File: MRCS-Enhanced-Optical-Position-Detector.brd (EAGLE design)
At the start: 45.6 x 30.3 mm, 17 parts, among them IC1 LM2903N, T1 PT19, T2 2N4401

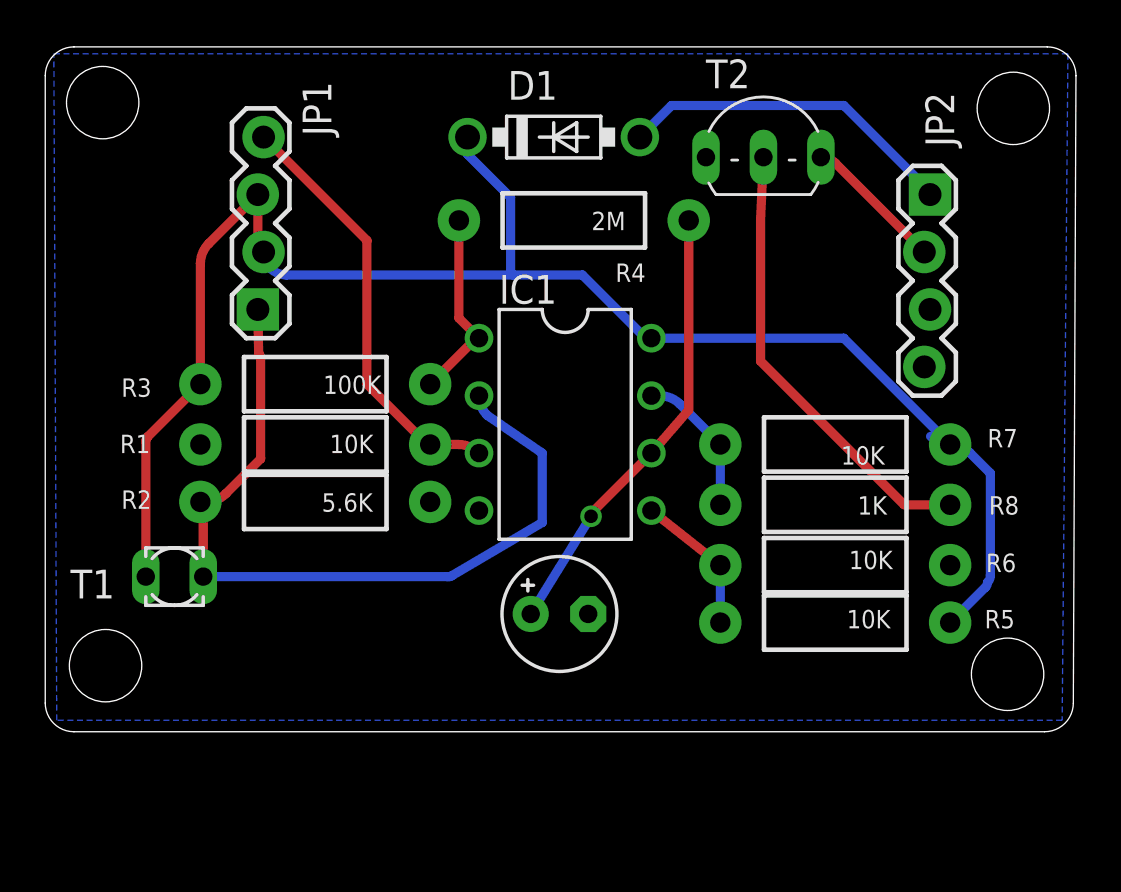
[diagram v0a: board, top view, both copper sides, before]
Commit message: clean up before panelizing
miscellaneous clean up of the file preperatory to panelizing
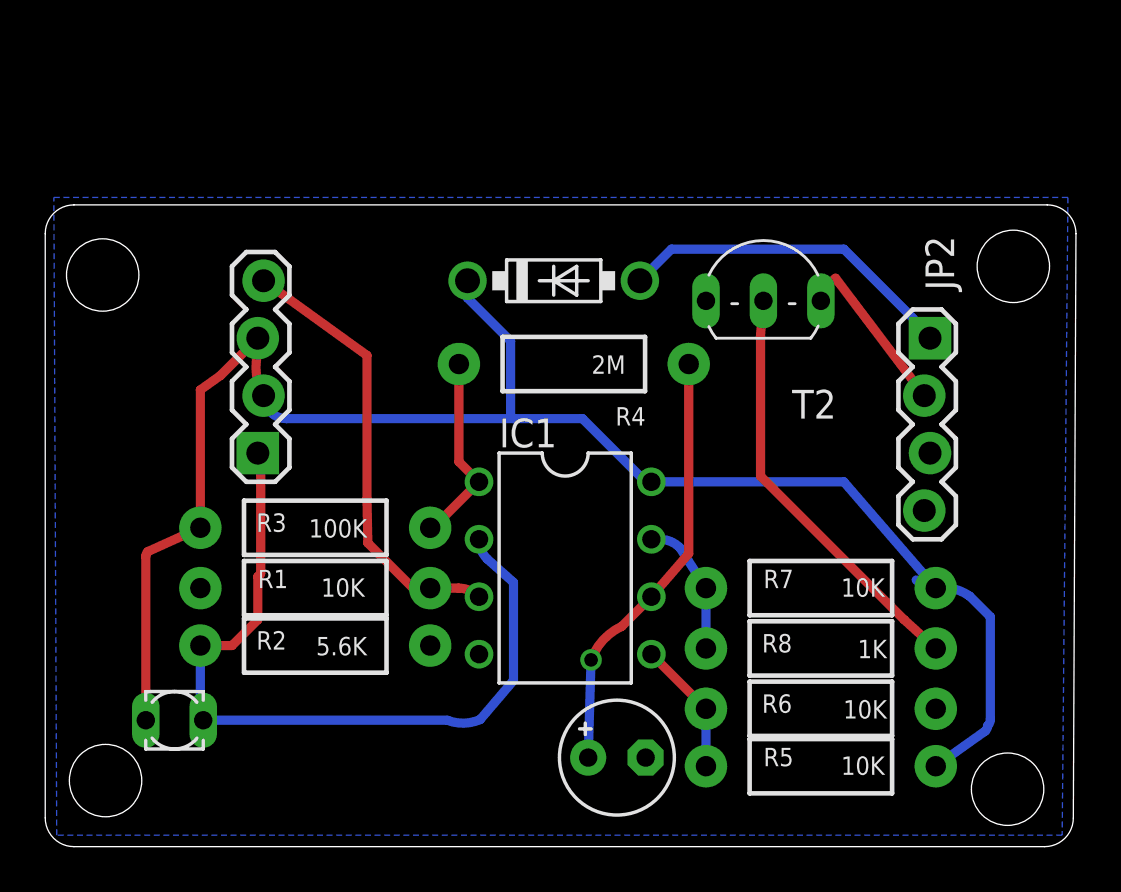
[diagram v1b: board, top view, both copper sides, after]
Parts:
- moved C1 6.84 mm to (25.4, 4.06)
- moved R6 6.38 mm to (34.4, 6.22)
- moved R5 6.38 mm to (34.4, 3.68)
- moved R7 6.38 mm to (34.4, 11.6)
- moved R8 6.38 mm to (34.4, 8.89)
- moved JP1 6.35 mm to (9.65, 17.5)
- moved R2 6.35 mm to (12.1, 9.02)
- moved R3 6.35 mm to (12.1, 14.2)
- moved U$3 6.35 mm to (35.7, 16.9)
- moved IC1 6.35 mm to (23.1, 12.4)
- moved R1 6.35 mm to (12.1, 11.6)
- moved T1 6.35 mm to (5.84, 5.71)
- moved D1 6.35 mm to (22.6, 25.1)
- moved JP2 6.35 mm to (39.1, 22.6)
- moved R4 6.35 mm to (23.5, 21.5)
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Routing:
- net N$8: track 6.25 -> 7.70 mm
- net N$7: track 20.0 -> 18.6 mm
- net VCC: track 72.7 -> 74.0 mm
- net N$3: track 18.9 -> 19.9 mm
- net N$2: track 19.9 -> 19.1 mm
- net N$1: track 35.9 -> 35.2 mm
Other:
- board size 45.6 x 30.3 mm -> 45.6 x 28.4 mm
- board text added: "EOPD Geoff Bunza 2015, Seth Neumann 2020"
- board text added: "rev 4 20201119"
- board text removed: "EOPD Geoff Bunza 2015, Seth Neumann 2017"
- board text removed: "rev 3 20180116"
